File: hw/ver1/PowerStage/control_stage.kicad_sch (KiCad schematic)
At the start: 51 parts, among them J10 SWD Debug, J11 BMS_Serial, J8 FanConnector, P1 USB_C_Plug_USB2.0, SW3 Boot, SW4 Reset, U10 RP2040, U20 W25Q32JVZP, U21 LM1117MP-5.0, U4 LM1117MP-3.3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

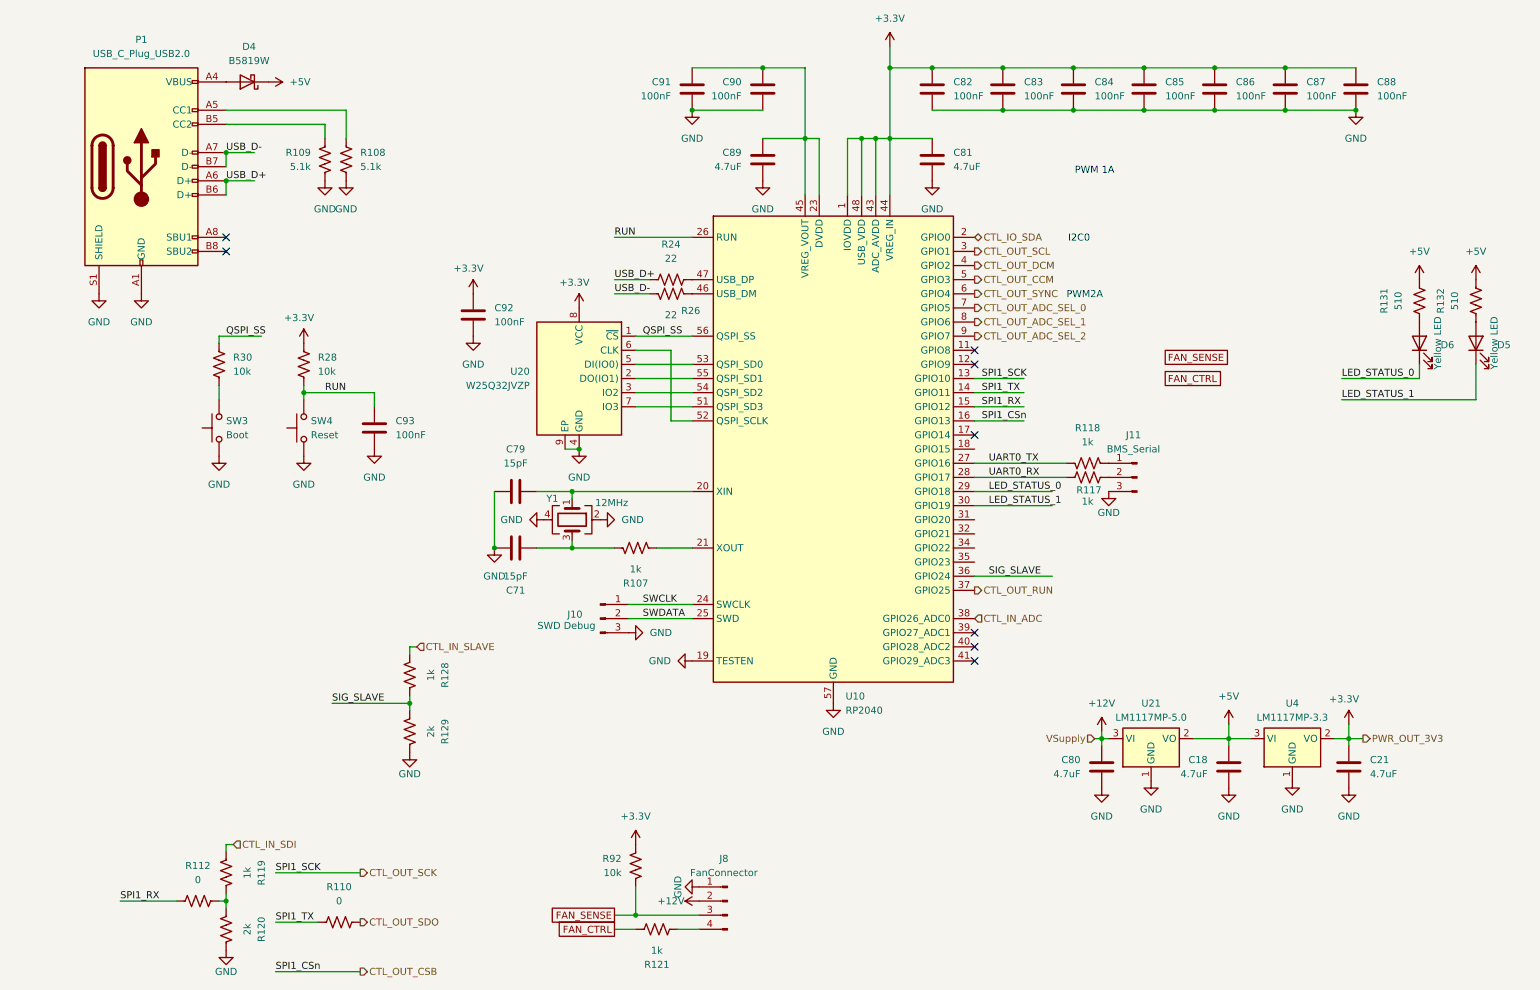
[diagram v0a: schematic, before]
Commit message: Finish the initial route before DRC
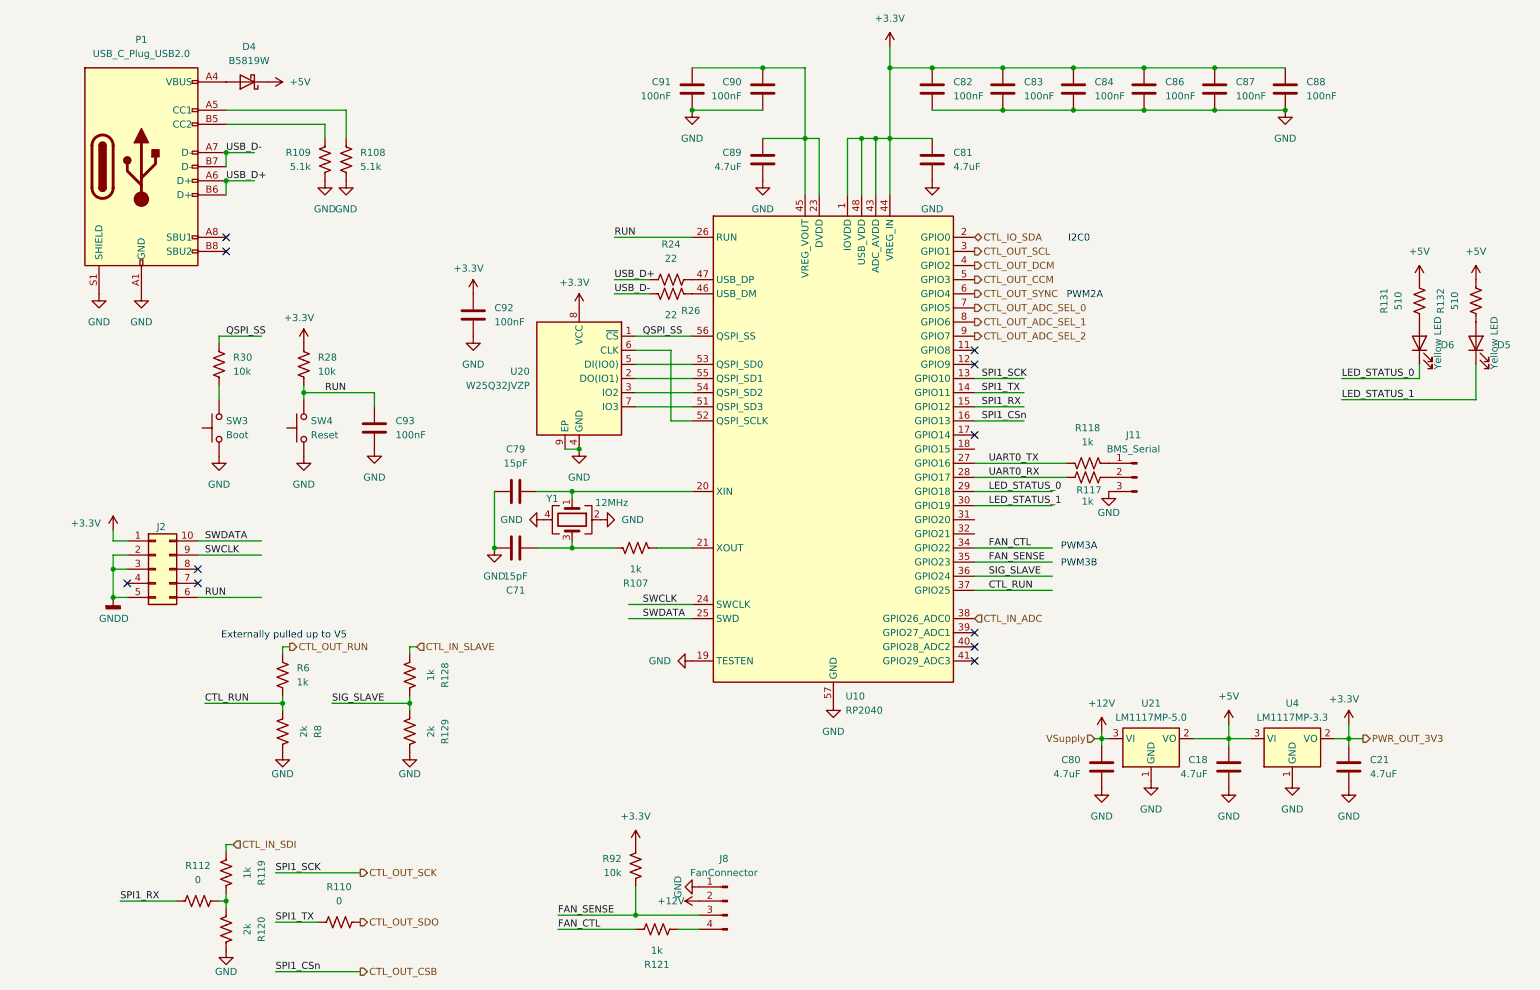
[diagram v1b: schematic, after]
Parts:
- removed C85: 100nF, Capacitor_SMD:C_0603_1608Metric, symbol Device:C
- removed J10: SWD Debug, Connector_PinHeader_2.54mm:PinHeader_1x03_P2.54mm_Vertical, symbol Connector:Conn_01x03_Pin
- added J2: ~, Connectors:JTAG_2x05_P1_27mm_Shrouded_SMD, symbol Connector_Generic:Conn_02x05_Counter_Clockwise
- added R6: 1k, Resistor_SMD:R_0603_1608Metric, symbol Device:R_US
- added R8: 2k, Resistor_SMD:R_0603_1608Metric, symbol Device:R_US
- J11: footprint Connector_PinHeader_2.54mm:PinHeader_1x03_P2.54mm_Vertical -> Connector_Harwin:Harwin_M20-89003xx_1x03_P2.54mm_Horizontal; Digikey N/A -> 952-3232-ND
- Y1: footprint Crystal:Crystal_SMD_3225-4Pin_3.2x2.5mm_HandSoldering -> Crystal:Crystal_SMD_3225-4Pin_3.2x2.5mm
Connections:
- net FAN_CTRL is gone; now on net FAN_CTL: R121.2
- net +3.3V: now also J2.1 (Pin_1)
- net CTL_OUT_RUN: now also R6.2; no longer U10.37 (GPIO25)
- net FAN_SENSE: now also U10.35 (GPIO23)
- net GND: now also R8.1
- net RUN: now also J2.6 (Pin_6)
- net SWCLK: now also J2.9 (Pin_9)
- net SWDATA: now also J2.10 (Pin_10)
- net FAN_CTL: now reaches U10.34 (GPIO22)
- new net CTL_RUN: R6.1, R8.2, U10.37 (GPIO25)
- new net GNDD: J2.2 (Pin_2), J2.3 (Pin_3), J2.5 (Pin_5)
- no-connect marks 8 -> 11
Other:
- note added: "Externally pulled up to V5"
- note added: "PWM3A"
- note added: "PWM3B"
- note removed: "PWM 1A"
- moved on the sheet: C86, C87, C88

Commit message: Resolve DRC errors
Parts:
- added D2, D7: Green LED, LED_SMD:LED_0805_2012Metric, symbol Device:LED
- added R10, R9: 510, Resistor_SMD:R_0603_1608Metric, symbol Device:R_US
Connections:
- net +3.3V: now also R10.1, R9.1
- net LED_STATUS_2: now reaches U10.31 (GPIO20)
- net LED_STATUS_2: now also D2.1 (K)
- net LED_STATUS_3: now reaches U10.32 (GPIO21)
- net LED_STATUS_3: now also D7.1 (K)
- new net: D2.2 (A), R9.2
- new net: D7.2 (A), R10.2
- no-connect marks 11 -> 12
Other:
- moved on the sheet: D5, D6, R131, R132

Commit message: Sync lunch work
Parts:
- U10, U20: JLCPCB Rotation Offset (none) -> -90
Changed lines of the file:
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@@
+			)
+		)
+		(property "JLCPCB Rotation Offset" "-90"
+			(at 110.49 81.28 0)
+			(effects
+				(font
+					(size 1.27 1.27)
+				)
+				(hide yes)
 			)
 		)
@@
 			(at 156.21 93.98 0)
 			(effects
+				(font
+					(size 1.27 1.27)
+				)
+				(hide yes)
+			)
+		)
+		(property "JLCPCB Rotation Offset" "-90"
+			(at 156.21 93.98 0)
+			(effects

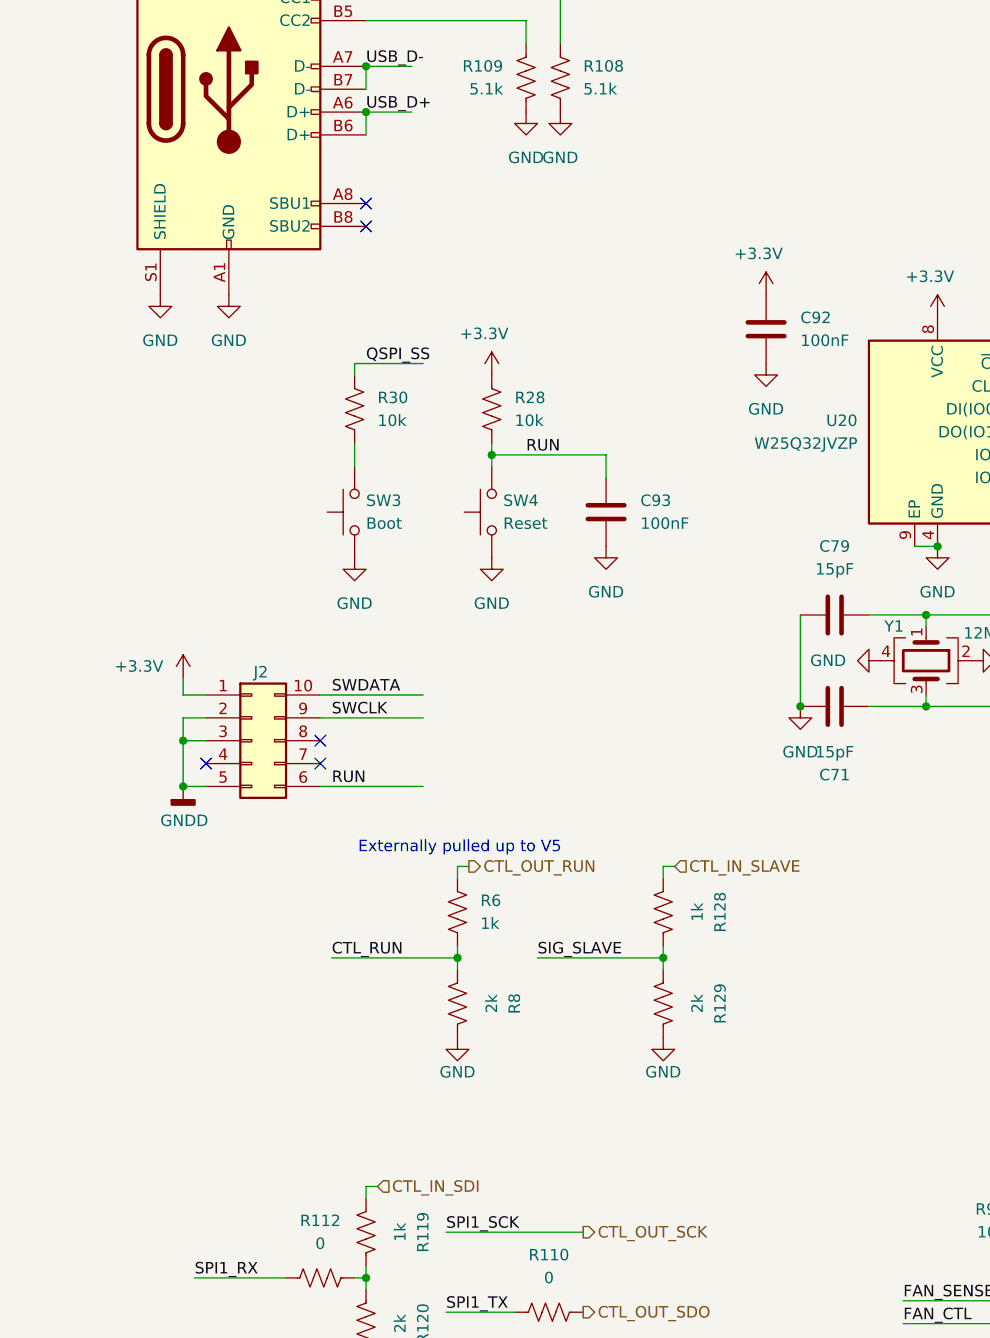
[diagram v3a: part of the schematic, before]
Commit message: Add driver support for V1 of the board. Revision HW to v2.0.
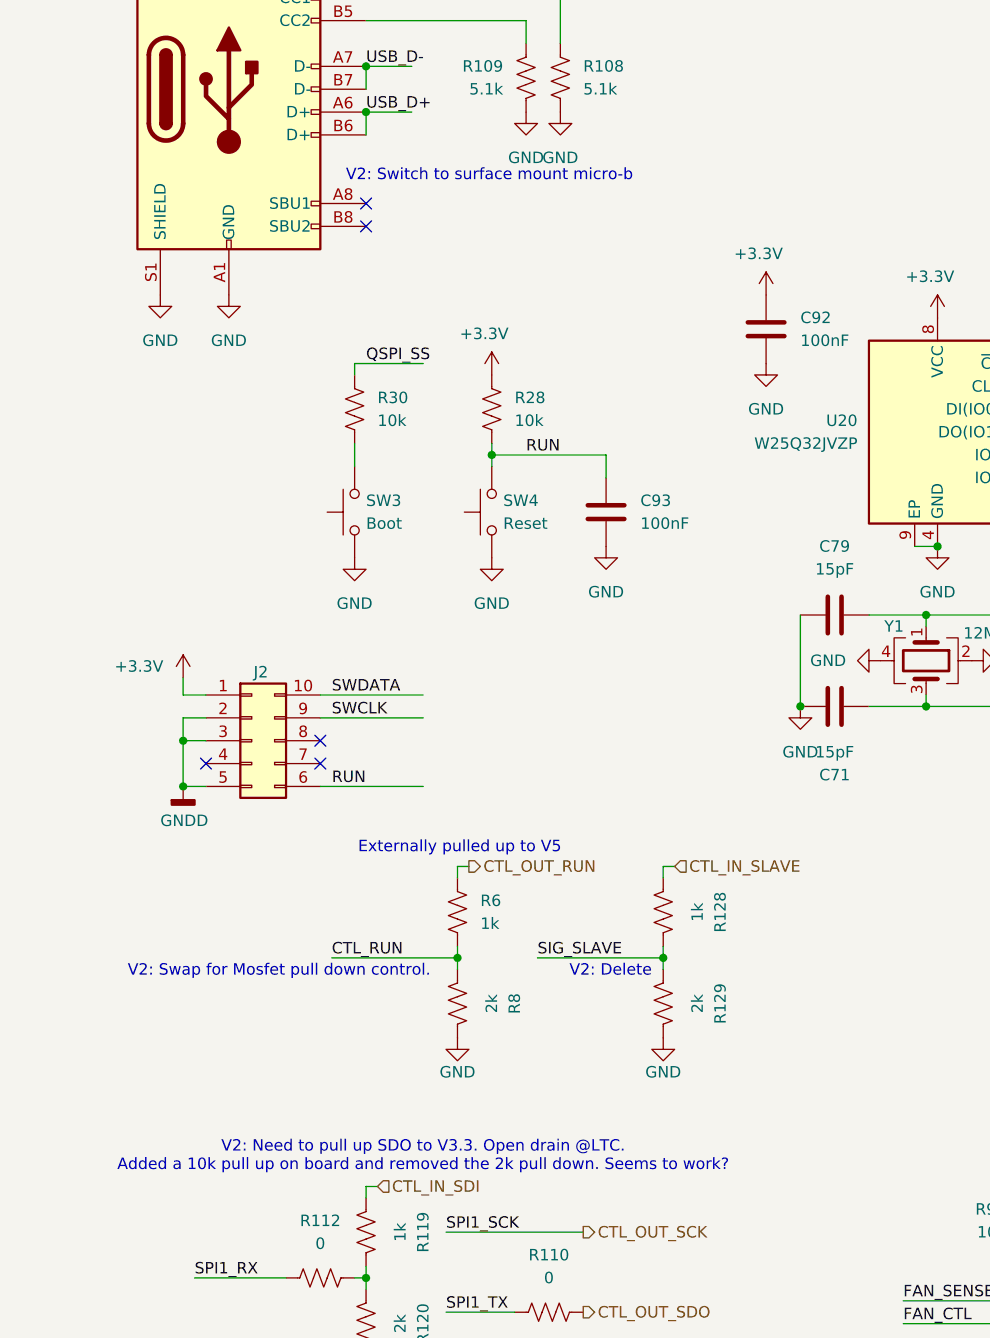
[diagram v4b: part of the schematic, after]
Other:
- note added: "V2: Delete"
- note added: "V2: Need to pull up SDO to V3.3. Open drain @LTC. Added a 10k pull up on board and removed the 2k pull down. Seems to work?"
- note added: "V2: Swap for Mosfet pull down control."
- note added: "V2: Switch to surface mount micro-b"
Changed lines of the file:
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@@
+		)
+	)
+	(text "V2: Delete"
+		(exclude_from_sim no)
+		(at 74.168 141.224 0)
+		(effects
+			(font
+				(size 1.27 1.27)
+			)
+		)
+	)
+	(text "V2: Switch to surface mount micro-b"
+		(exclude_from_sim no)
+		(at 60.706 52.832 0)
+		(effects
+			(font
+				(size 1.27 1.27)
+			)
 		)
 	)
@@
 		)
 	)
+	(text "V2: Swap for Mosfet pull down control."
+		(exclude_from_sim no)
+		(at 37.338 141.224 0)
+		(effects
+			(font
+				(size 1.27 1.27)
+			)
+		)
+	)
 	(text "PWM3B"
 		(exclude_from_sim no)
@@
 		(effects
 			(font
+				(size 1.27 1.27)
+			)
+		)
+	)
+	(text "V2: Need to pull up SDO to V3.3. Open drain @LTC.\nAdded a 10k pull up on board and removed the 2k pull down. Seems to work?"
+		(exclude_from_sim no)
+		(at 53.34 161.798 0)
+		(effects
+			(font
